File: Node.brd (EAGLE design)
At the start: 38.1 x 38.1 mm, 64 parts, among them J1 DF12A3.0-14DS, Q1 16MHz, U1 ATMEGA32U4QFN, U2 NRF24L01NOPAD, U3 LTC3553, U4 L3GD20, U6 LSM303DLHC, U7 BD2425NNRF0404, U9 RCLAMP0502A, X1 USB-FCI

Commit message: start of 0.3 layout
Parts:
- removed C27: TBD, SparkFun:0402-CAP
- removed L3: TBD, adjacent-reality:C0402
- removed OSHW: (no value), ohw-logo:OSHW_FILLX200_NOTEXT
- removed U$2: (no value), SparkFun-Electromechanical:STAND-OFF
- BAT: value (none) -> LR2450; device SparkFun-Electromechanical:BATTCON_245MM_PTH -> adjacent-reality:BATTCON_245MM_SLOT
- U$1: device SparkFun-Electromechanical:STAND-OFF -> SparkFun-Electromechanical:STAND-OFF-TIGHT
- moved RF 123.9 mm to (3.02, 25.9)
- moved U7 110.1 mm to (5.17, 21.8)
- moved L2 106.7 mm to (3.97, 22.5), turned to 90 degrees
- moved C26 94.8 mm to (7.14, 22.9)
- moved C25 89.9 mm to (7.14, 21.7)
- moved C24 83.2 mm to (1.91, 19.4), turned to 90 degrees
- moved J1 79.6 mm to (20.2, 25.1)
- moved C22 79.3 mm to (0.79, 19.4), turned to 90 degrees
- moved R4 65.3 mm to (8.10, 19.5), turned to 90 degrees
- moved Q1 63.2 mm to (9.68, 19.5), turned to 90 degrees
- moved BAT 41.1 mm to (14.0, 14.0), flipped to the bottom
- moved R3 33.8 mm to (1.91, 21.6)
- moved HWB 33.0 mm to (26.7, 1.27), flipped to the bottom
- moved R10 31.3 mm to (5.71, 12.1)
- moved R11 30.5 mm to (6.99, 12.1), turned to 90 degrees
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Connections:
- removed net N$31: C27.1, L2.2, L3.1
- net BUCK_ON: now also U3.7
- net GND: now also BAT.GND; no longer BAT.2, C27.2
- net N$29: now also BAT.+1, BAT.+2, BAT.+3, BAT.+4; no longer BAT.3
- net N$30: now also L2.2; no longer L3.2
- net N$8: now also U3.4
- net RESET: now also U3.3
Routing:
- net +3V3: track 171.9 -> 54.0 mm, vias 5 -> 0
- net RESET: track 10.8 -> 46.7 mm, vias 0 -> 2
- net SCL: track 34.5 -> 1.40 mm, vias 4 -> 0
- net GND: track 34.1 -> 5.92 mm, vias 31 -> 0
- net N$1: track 47.0 -> 20.0 mm, vias 4 -> 2
- net SDA: track 29.9 -> 3.13 mm, vias 2 -> 0
- net N$8: track 2.58 -> 29.2 mm, vias 0 -> 2
- net PCINT4: track 23.7 -> 0.00 mm, vias 2 -> 0
- net N$16: track 24.7 -> 1.24 mm, vias 4 -> 0
- net MOSI: track 16.7 -> 0.00 mm, vias 1 -> 0
- net SCK: track 15.1 -> 0.00 mm, vias 1 -> 0
- net VBUS: track 47.8 -> 34.1 mm, vias 4 -> 0
- net PCINT5: track 10.8 -> 0.00 mm, vias 2 -> 0
- net N$4: track 0.00 -> 9.49 mm
- net VDIV: track 9.00 -> 1.27 mm
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- removed copper zone on layer 1, net GND
- removed copper zone on layer 16, net GND
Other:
- board size 38.1 x 38.1 mm -> 27.9 x 27.9 mm
- board text removed: "+"
- board text removed: "3V3"
- board text removed: "AVR ISP"
- board text removed: "BT_R"
- board text removed: "F0"
- board text removed: "F1"
- board text removed: "F4"
- board text removed: "F5"
- board text removed: "F6"
- board text removed: "F7"
- board text removed: "GND"
- board text removed: "HWB"
- board text removed: "RXI"
- board text removed: "TXO"
- board text removed: "VBUS"
- board text removed: "VIN"
- board text removed: "X"
- board text removed: "Y"
- board text removed: "Z"

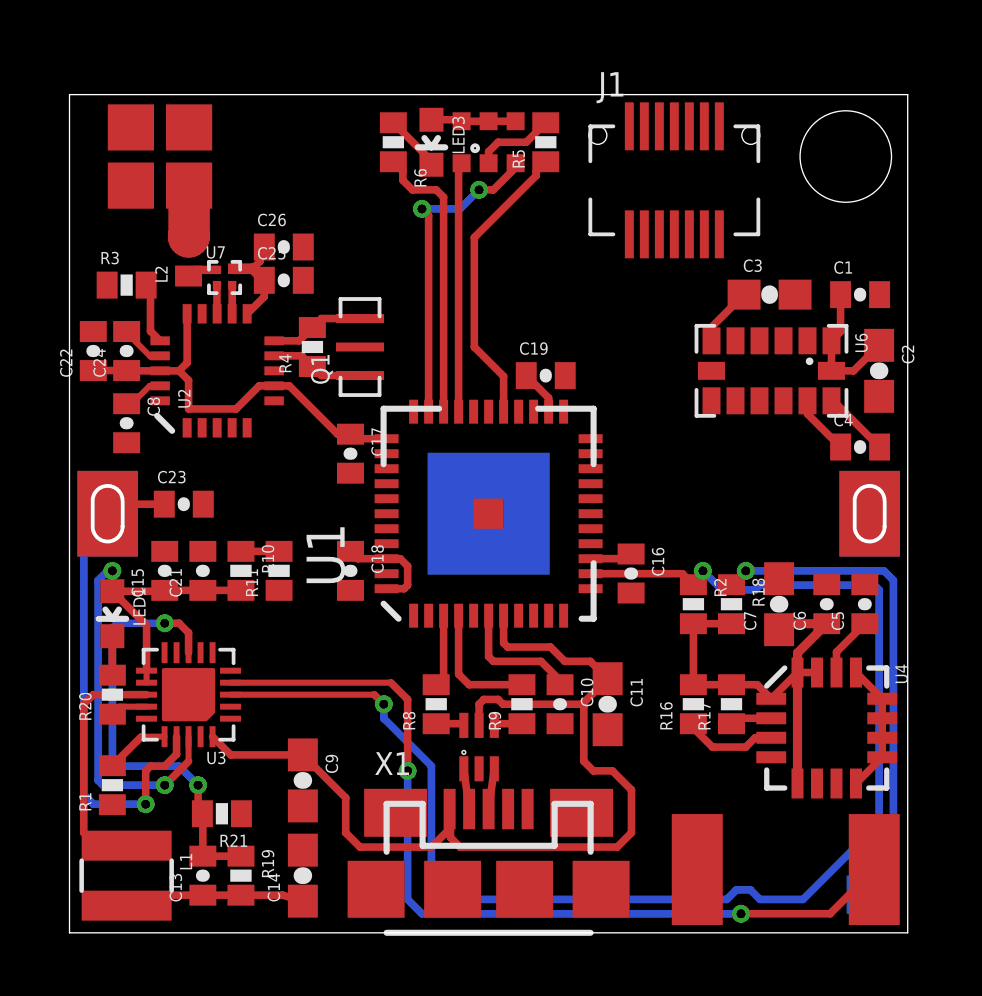
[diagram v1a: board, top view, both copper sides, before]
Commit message: start of base station layout
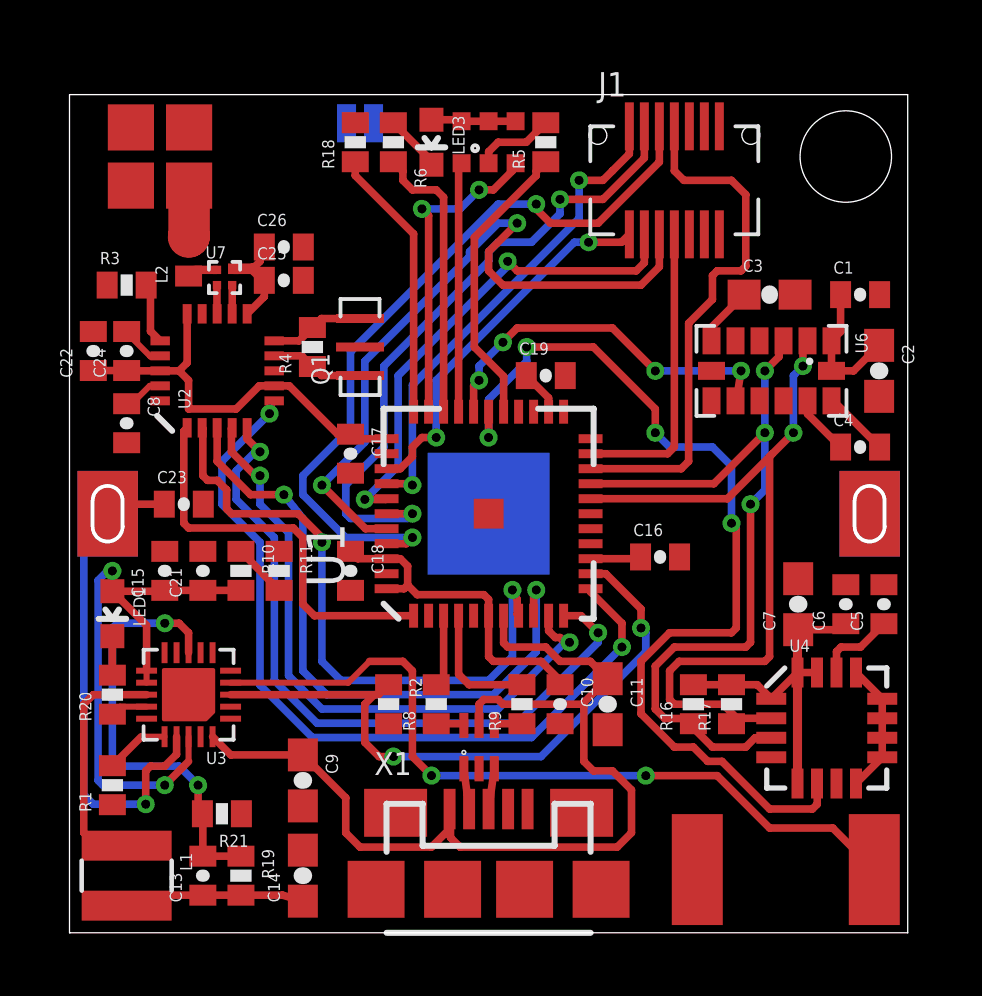
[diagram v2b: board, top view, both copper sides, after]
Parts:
- moved HWB 30.8 mm to (9.68, 27.0)
- moved R18 19.9 mm to (9.53, 26.4), turned to 90 degrees
- moved R2 10.7 mm to (10.6, 7.62)
- moved C16 1.11 mm to (19.7, 12.5), turned to 0 degrees
- moved C7 0.64 mm to (24.3, 11.0)
- moved C5 0.63 mm to (27.1, 11.0)
- moved C6 0.63 mm to (25.9, 11.0)
- turned R11 to 270 degrees
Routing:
- net PCINT4: track 0.00 -> 32.1 mm, vias 0 -> 4
- net PCINT7: track 0.00 -> 27.1 mm, vias 0 -> 2
- net A0: track 0.00 -> 25.3 mm, vias 0 -> 2
- net RESET: track 46.7 -> 21.8 mm
- net SCL: track 1.40 -> 26.0 mm, vias 0 -> 2
- net A1: track 0.00 -> 23.8 mm, vias 0 -> 2
- net MISO: track 0.00 -> 23.8 mm, vias 0 -> 2
- net SDA: track 3.13 -> 26.6 mm, vias 0 -> 3
- net A4: track 0.00 -> 21.7 mm, vias 0 -> 2
- net SCK: track 0.00 -> 21.6 mm, vias 0 -> 2
- net MOSI: track 0.00 -> 21.3 mm, vias 0 -> 2
- net SS: track 0.00 -> 21.0 mm, vias 0 -> 2
- net RX: track 0.00 -> 17.7 mm
- net A5: track 0.00 -> 16.4 mm, vias 0 -> 2
- net A6: track 0.00 -> 16.3 mm, vias 0 -> 2
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
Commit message: a few more painful wires
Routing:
- net BUCK_ON: track 0.00 -> 50.9 mm, vias 0 -> 5
- net SCK: track 21.6 -> 49.3 mm, vias 2 -> 3
- net MISO: track 23.8 -> 51.4 mm, vias 2 -> 4
- net RESET: track 21.8 -> 44.4 mm, vias 2 -> 4
- net MOSI: track 21.3 -> 42.4 mm, vias 2 -> 4
- net VDIV: track 1.82 -> 19.9 mm, vias 0 -> 2
- net STBY: track 0.00 -> 17.3 mm, vias 0 -> 2
- net +3V3: track 53.2 -> 61.7 mm, vias 0 -> 2
- net HWB: track 9.14 -> 10.8 mm, vias 0 -> 1

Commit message: so close
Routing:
- net GND: track 5.92 -> 61.8 mm, vias 0 -> 29
- net +3V3: track 61.7 -> 100.0 mm, vias 2 -> 7
- net MOSI: track 42.4 -> 44.9 mm
- net PCINT5: track 12.5 -> 13.8 mm
- net SDA: track 26.6 -> 25.8 mm
- added copper zone on layer 1, net GND
- added copper zone on layer 16, net GND

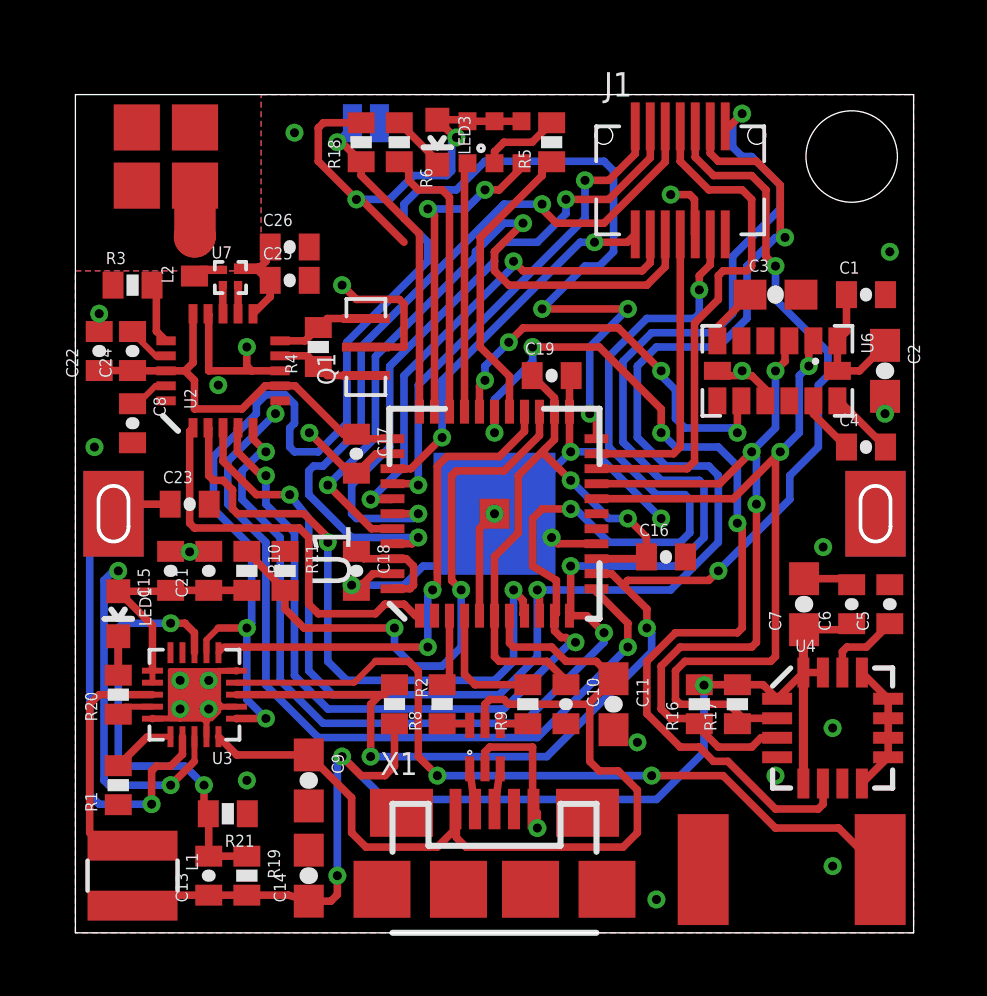
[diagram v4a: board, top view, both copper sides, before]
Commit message: the slow and steady march to zero airwires
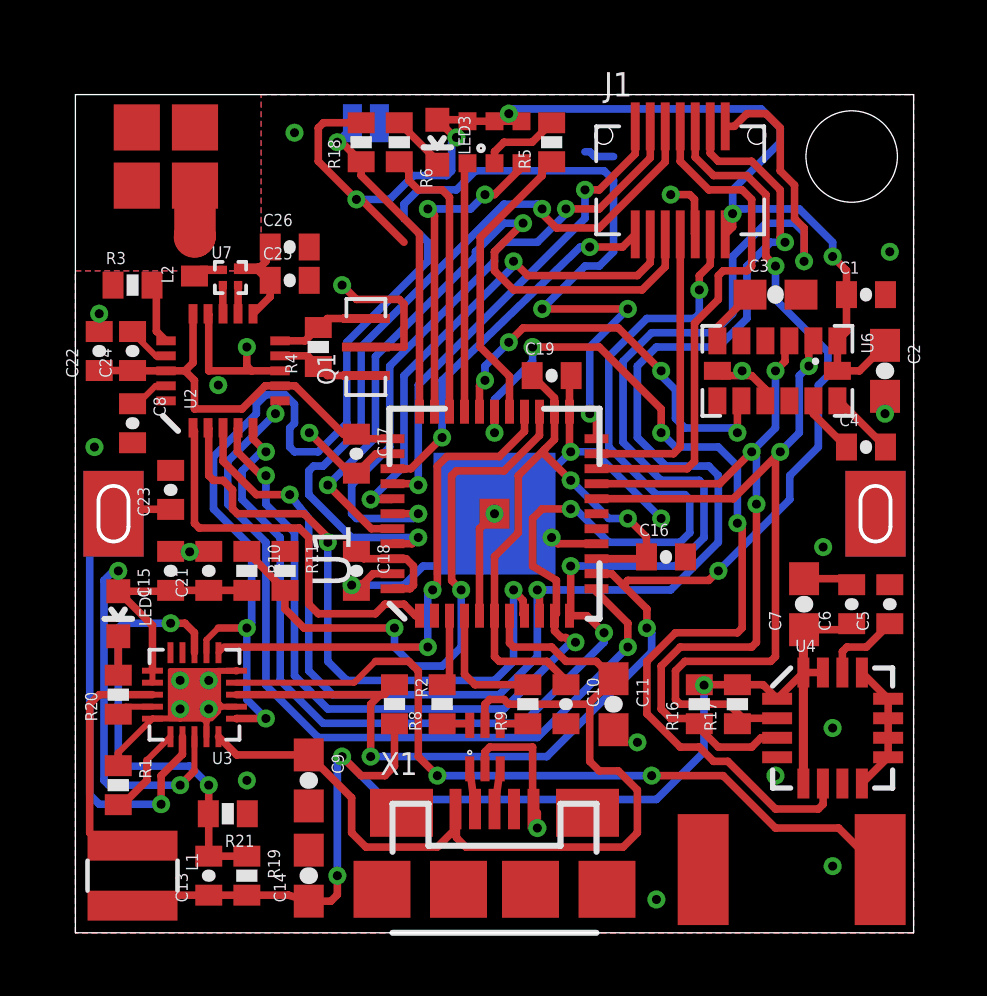
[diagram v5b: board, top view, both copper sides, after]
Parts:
- moved C23 0.79 mm to (3.17, 14.8), turned to 90 degrees
- turned R1 to 270 degrees
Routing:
- net +3V3: track 100.0 -> 120.0 mm, vias 7 -> 10
- net MISO: track 51.3 -> 55.0 mm
- net GND: track 61.8 -> 64.8 mm
- net N$2: track 2.14 -> 3.07 mm

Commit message: 7 more to go
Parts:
- turned R11 to 90 degrees
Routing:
- net GND: track 64.8 -> 67.9 mm
- net CE: track 13.5 -> 12.1 mm
- net SS: track 21.0 -> 20.5 mm
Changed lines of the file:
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@@
 <element name="R20" library="SparkFun" package="0402-RES" value="1k" x="1.42875" y="7.9375" rot="R90"/>
 <element name="R10" library="SparkFun" package="0402-RES" value="100k" x="5.715" y="12.065" rot="R270"/>
-<element name="R11" library="SparkFun" package="0402-RES" value="100k" x="6.985" y="12.065" rot="R270"/>
+<element name="R11" library="SparkFun" package="0402-RES" value="100k" x="6.985" y="12.065" rot="R90"/>
 <element name="R1" library="SparkFun" package="0402-RES" value="7.5k" x="1.42875" y="4.92125" rot="R270"/>
 <element name="C13" library="SparkFun" package="0402-CAP" value="10pF" x="4.445" y="1.905" rot="R90"/>
@@
 <wire x1="17.145" y1="26.035" x2="17.30375" y2="25.87625" width="0.254" layer="16"/>
 <wire x1="17.30375" y1="25.87625" x2="17.93875" y2="25.87625" width="0.254" layer="16"/>
+<wire x1="6.985" y1="11.415" x2="6.985" y2="11.43" width="0.254" layer="1"/>
+<wire x1="6.985" y1="11.43" x2="6.35" y2="12.065" width="0.254" layer="1"/>
+<wire x1="6.35" y1="12.065" x2="5.095" y2="12.065" width="0.254" layer="1"/>
+<wire x1="5.095" y1="12.065" x2="4.445" y2="12.715" width="0.254" layer="1"/>
 <wire x1="27.0025" y1="21.2725" x2="24.18625" y2="21.2725" width="0" layer="19" extent="1-1"/>
-<wire x1="6.985" y1="12.715" x2="9.2075" y2="11.57375" width="0" layer="19" extent="1-1"/>
 </signal>
 <signal name="+3V3">
@@
 <contactref element="R11" pad="2"/>
 <contactref element="U1" pad="25"/>
-<wire x1="6.985" y1="11.415" x2="5.715" y2="12.715" width="0.254" layer="1"/>
+<wire x1="6.985" y1="12.715" x2="5.715" y2="12.715" width="0.254" layer="1"/>
 <wire x1="15.47" y1="17.37" x2="15.47" y2="16.58125" width="0.254" layer="1"/>
 <wire x1="15.47" y1="16.58125" x2="14.2875" y2="15.39875" width="0.254" layer="1"/>
@@
 <wire x1="10.63625" y1="9.525" x2="10.63625" y2="10.16" width="0.254" layer="16"/>
 <via x="10.63625" y="10.16" extent="1-16" drill="0.3"/>
-<wire x1="10.63625" y1="10.16" x2="7.62" y2="10.16" width="0.254" layer="1"/>
-<wire x1="7.62" y1="10.16" x2="6.985" y2="10.795" width="0.254" layer="1"/>
-<wire x1="6.985" y1="10.795" x2="6.985" y2="11.415" width="0.254" layer="1"/>
+<wire x1="10.63625" y1="10.16" x2="8.5725" y2="10.16" width="0.254" layer="1"/>
+<wire x1="8.5725" y1="10.16" x2="7.9375" y2="10.795" width="0.254" layer="1"/>
+<wire x1="7.9375" y1="10.795" x2="7.9375" y2="11.7475" width="0.254" layer="1"/>
+<wire x1="7.9375" y1="11.7475" x2="6.985" y2="12.715" width="0.254" layer="1"/>
 </signal>
 <signal name="N$29">
@@
 <wire x1="9.04875" y1="19.685" x2="9.04875" y2="16.98625" width="0.254" layer="16"/>
 <wire x1="9.04875" y1="16.98625" x2="8.09625" y2="16.03375" width="0.254" layer="16"/>
-<wire x1="8.09625" y1="16.03375" x2="7.3025" y2="16.03375" width="0.254" layer="16"/>
-<wire x1="7.3025" y1="16.03375" x2="7.14375" y2="16.1925" width="0.254" layer="16"/>
-<wire x1="7.14375" y1="16.1925" x2="7.14375" y2="16.8275" width="0.254" layer="16"/>
+<wire x1="8.09625" y1="16.03375" x2="7.46125" y2="16.03375" width="0.254" layer="16"/>
+<wire x1="7.46125" y1="16.03375" x2="7.14375" y2="16.35125" width="0.254" layer="16"/>
+<wire x1="7.14375" y1="16.35125" x2="7.14375" y2="16.8275" width="0.254" layer="16"/>
 <wire x1="7.14375" y1="16.8275" x2="7.3025" y2="16.98625" width="0.254" layer="16"/>
 <wire x1="7.3025" y1="16.98625" x2="7.3025" y2="17.62125" width="0.254" layer="16"/>
@@
 <contactref element="U2" pad="2"/>
 <wire x1="4.42125" y1="16.8325" x2="4.445" y2="16.80875" width="0.254" layer="1"/>
-<wire x1="4.445" y1="16.80875" x2="4.445" y2="15.24" width="0.254" layer="1"/>
-<wire x1="4.445" y1="15.24" x2="4.60375" y2="15.08125" width="0.254" layer="1"/>
-<wire x1="4.60375" y1="15.08125" x2="4.92125" y2="15.08125" width="0.254" layer="1"/>
-<wire x1="4.92125" y1="15.08125" x2="5.23875" y2="14.76375" width="0.254" layer="1"/>
-<wire x1="5.23875" y1="14.76375" x2="5.23875" y2="14.12875" width="0.254" layer="1"/>
-<wire x1="5.23875" y1="14.12875" x2="5.3975" y2="13.97" width="0.254" layer="1"/>
-<wire x1="5.3975" y1="13.97" x2="7.62" y2="13.97" width="0.254" layer="1"/>
+<wire x1="4.445" y1="16.80875" x2="4.445" y2="15.5575" width="0.254" layer="1"/>
+<wire x1="4.445" y1="15.5575" x2="6.0325" y2="13.97" width="0.254" layer="1"/>
+<wire x1="6.0325" y1="13.97" x2="7.62" y2="13.97" width="0.254" layer="1"/>
 <wire x1="7.62" y1="13.97" x2="8.41375" y2="13.17625" width="0.254" layer="1"/>
 <wire x1="8.41375" y1="13.17625" x2="8.41375" y2="13.0175" width="0.254" layer="1"/>
@@
 <contactref element="U2" pad="1"/>
 <wire x1="3.92125" y1="16.8325" x2="3.96875" y2="16.72125" width="0.254" layer="1"/>
-<wire x1="3.96875" y1="16.72125" x2="3.96875" y2="13.6525" width="0.254" layer="1"/>
-<wire x1="3.96875" y1="13.6525" x2="4.1275" y2="13.49375" width="0.254" layer="1"/>
-<wire x1="4.1275" y1="13.49375" x2="7.46125" y2="13.49375" width="0.254" layer="1"/>
+<wire x1="3.96875" y1="16.72125" x2="3.96875" y2="15.39875" width="0.254" layer="1"/>
+<wire x1="3.96875" y1="15.39875" x2="5.87375" y2="13.49375" width="0.254" layer="1"/>
+<wire x1="5.87375" y1="13.49375" x2="7.46125" y2="13.49375" width="0.254" layer="1"/>
 <wire x1="7.46125" y1="13.49375" x2="7.77875" y2="13.17625" width="0.254" layer="1"/>
-<wire x1="7.77875" y1="13.17625" x2="7.77875" y2="10.95375" width="0.254" layer="1"/>
-<wire x1="7.77875" y1="10.95375" x2="8.09625" y2="10.63625" width="0.254" layer="1"/>
-<wire x1="8.09625" y1="10.63625" x2="10.00125" y2="10.63625" width="0.254" layer="1"/>
+<wire x1="7.77875" y1="13.17625" x2="7.77875" y2="12.7" width="0.254" layer="1"/>
+<wire x1="7.77875" y1="12.7" x2="8.41375" y2="12.065" width="0.254" layer="1"/>
+<wire x1="8.41375" y1="12.065" x2="8.41375" y2="10.95375" width="0.254" layer="1"/>
+<wire x1="8.41375" y1="10.95375" x2="8.73125" y2="10.63625" width="0.254" layer="1"/>
+<wire x1="8.73125" y1="10.63625" x2="10.00125" y2="10.63625" width="0.254" layer="1"/>
 <wire x1="10.00125" y1="10.63625" x2="10.31875" y2="10.95375" width="0.254" layer="1"/>
 <wire x1="10.31875" y1="10.95375" x2="10.95375" y2="10.95375" width="0.254" layer="1"/>

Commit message: all of the real airwires?
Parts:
- moved R2 0.79 mm to (10.0, 7.14), turned to 0 degrees
- moved C14 0.16 mm to (7.62, 1.91)
- moved C9 0.16 mm to (7.62, 5.08)
- turned C2 to 90 degrees
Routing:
- net N$29: track 16.7 -> 61.2 mm
- net +3V3: track 120.0 -> 149.8 mm, vias 10 -> 16
- net GND: track 67.9 -> 71.1 mm
- net RESET: track 44.3 -> 42.3 mm, vias 4 -> 3
- net VDIV: track 20.0 -> 18.7 mm
- net N$8: track 26.5 -> 25.5 mm
- net STBY: track 17.3 -> 16.5 mm
- net BUCK_ON: track 49.8 -> 50.4 mm
